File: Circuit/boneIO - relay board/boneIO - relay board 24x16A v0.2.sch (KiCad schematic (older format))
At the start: 68 parts, among them J1 Screw_Terminal_01x04, J10 Screw_Terminal_01x04, J11 Screw_Terminal_01x04, J12 Screw_Terminal_01x04, J13 Screw_Terminal_01x04, J14 Conn_02x04_Odd_Even, J2 Screw_Terminal_01x04, J3 Conn_02x04_Odd_Even, J4 Screw_Terminal_01x04, J5 Screw_Terminal_01x04, J6 Screw_Terminal_01x04, J7 Screw_Terminal_01x04, J8 Screw_Terminal_01x04, J9 Screw_Terminal_01x04, K1 RM85-2011-35-1005, K10 RM85-2011-35-1005, K11 RM85-2011-35-1005, K12 RM85-2011-35-1005, K13 RM85-2011-35-1005, K14 RM85-2011-35-1005, K15 RM85-2011-35-1005, K16 RM85-2011-35-1005, K17 RM85-2011-35-1005, K18 RM85-2011-35-1005, K19 RM85-2011-35-1005, K2 RM85-2011-35-1005, K20 RM85-2011-35-1005, K21 RM85-2011-35-1005, K22 RM85-2011-35-1005, K23 RM85-2011-35-1005, K24 RM85-2011-35-1005, K3 RM85-2011-35-1005, K4 RM85-2011-35-1005, K5 RM85-2011-35-1005, K6 RM85-2011-35-1005, K7 RM85-2011-35-1005, K8 RM85-2011-35-1005, K9 RM85-2011-35-1005, SW1 SW_DIP_x03, SW2 SW_DIP_x03, SW3 SW_DIP_x03, U1 MCP9808_MSOP, U2 MCP23017_SS, U3 MCP23017_SS, U4 ULN2803A, U5 ULN2803A, U6 ULN2803A

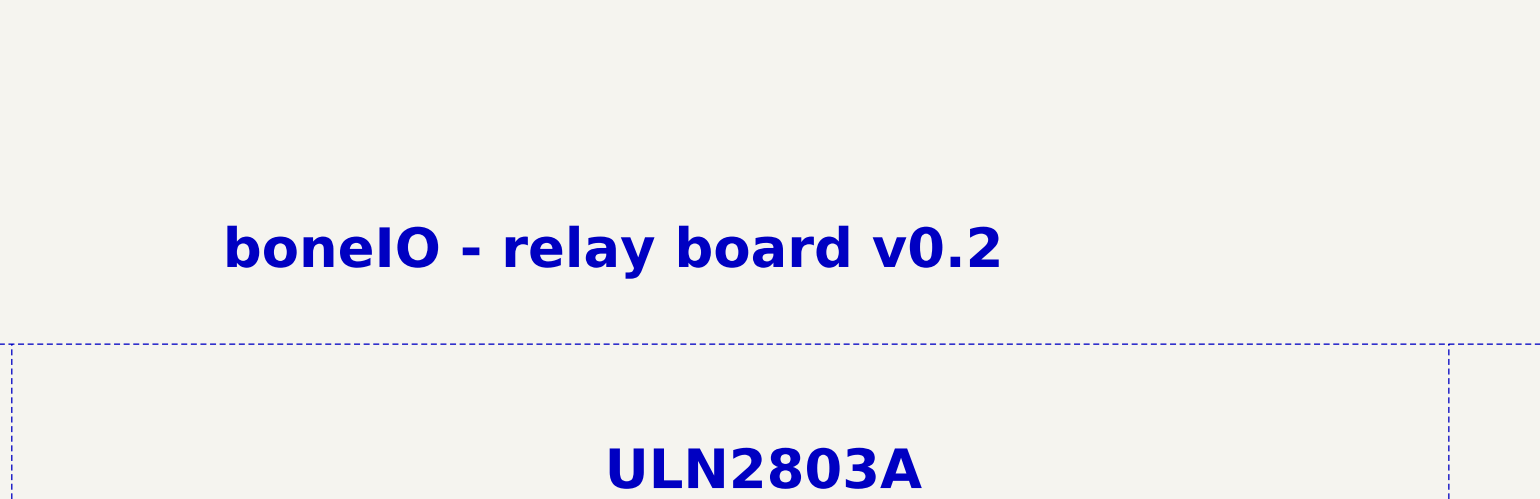
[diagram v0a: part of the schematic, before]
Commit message: Zmiana Nazwy płytki
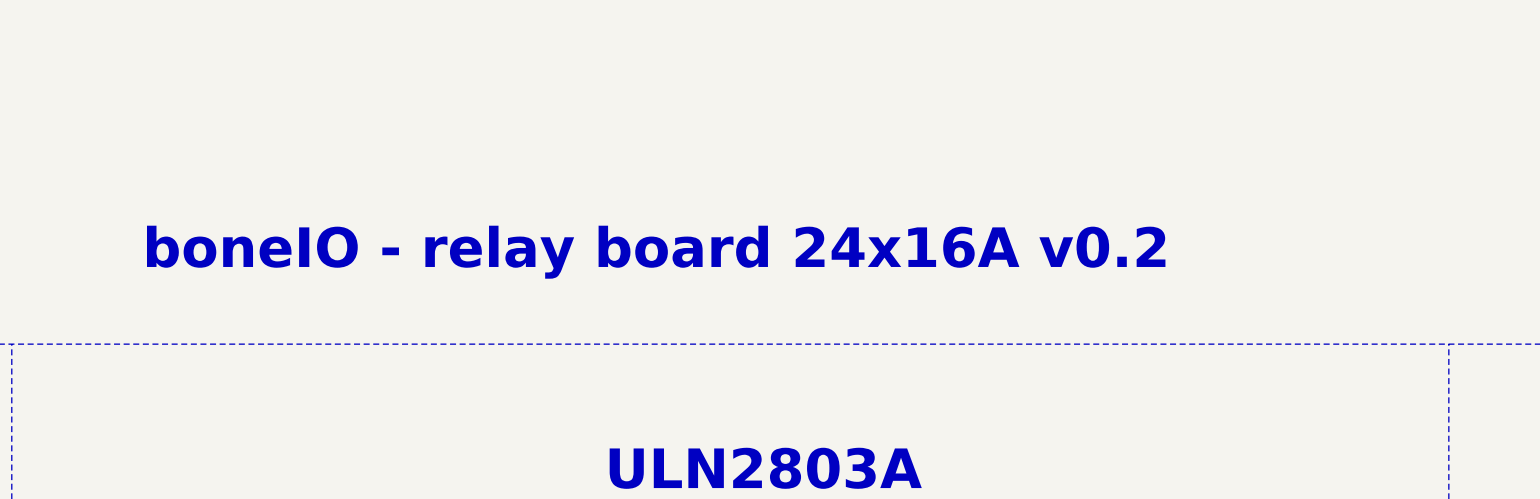
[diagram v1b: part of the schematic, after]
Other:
- note added: "boneIO - relay board 24x16A v0.2"
- note removed: "boneIO - relay board v0.2"
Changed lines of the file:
@@
 Text Notes 18650 2300 0    197  ~ 39
 MCP23017
-Text Notes 9600 1250 0    197  ~ 39
-boneIO - relay board v0.2
+Text Notes 9200 1250 0    197  ~ 39
+boneIO - relay board 24x16A v0.2
 Wire Wire Line
 	6750 100  6750 400
